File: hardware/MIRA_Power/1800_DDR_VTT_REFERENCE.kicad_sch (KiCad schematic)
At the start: 13 parts, among them Q1801 BSS138N, U1801 TPS51200DRCR

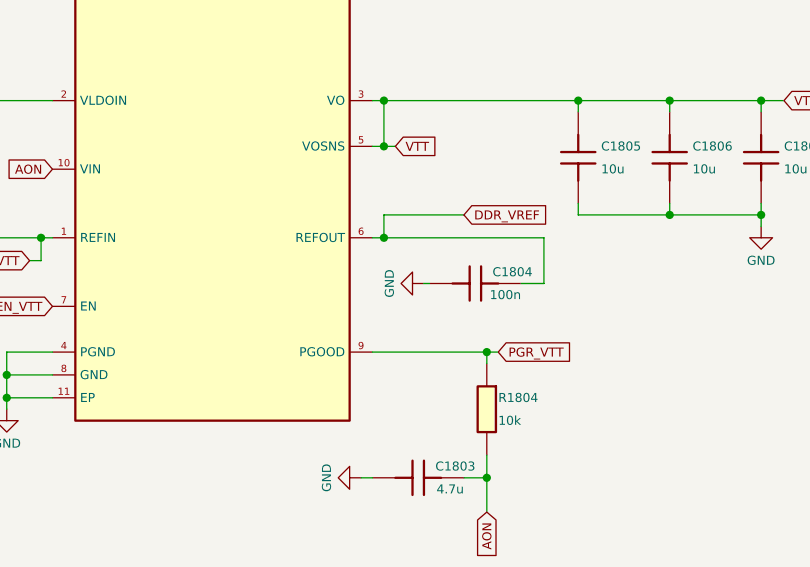
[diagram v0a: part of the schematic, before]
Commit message: Add high-load schematic candidate with CORE sense and revised N15 supply
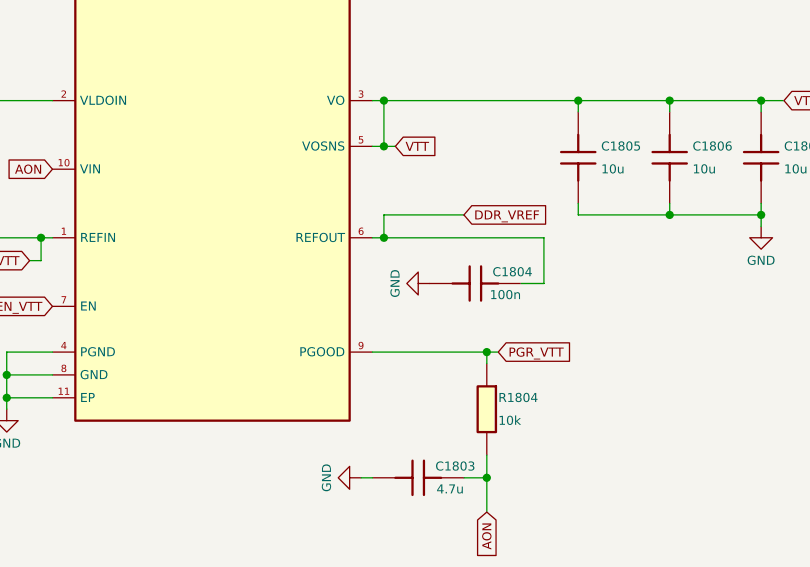
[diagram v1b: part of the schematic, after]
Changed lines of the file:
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@@
 	(wire
 		(pts
-			(xy 100.965 123.19) (xy 101.6 123.19)
+			(xy 101.6 123.19) (xy 101.6 123.19)
 		)
 		(stroke
@@
 	(symbol
 		(lib_id "power:GND")
-		(at 100.965 123.19 270)
+		(at 101.6 123.19 270)
 		(unit 1)
 		(body_style 1)
@@
 		(dnp no)
 		(property "Reference" "#PWR01805"
-			(at 100.965 123.19 0)
+			(at 101.6 123.19 0)
 			(hide yes)
 			(show_name no)
@@
 		)
 		(property "Value" "GND"
-			(at 97.155 123.19 0)
+			(at 97.79 123.19 0)
 			(show_name no)
 			(do_not_autoplace no)
@@
 		)
 		(property "Footprint" ""
-			(at 100.965 123.19 0)
+			(at 101.6 123.19 0)
 			(show_name no)
 			(do_not_autoplace no)
@@
 		)
 		(property "Datasheet" ""
-			(at 100.965 123.19 0)
+			(at 101.6 123.19 0)
 			(show_name no)
 			(do_not_autoplace no)
@@
 		)
 		(property "Description" ""
-			(at 100.965 123.19 0)
-			(show_name no)
-			(do_not_autoplace no)
+			(at 101.6 123.19 0)
+			(show_name no)
+			(do_not_autoplace no)

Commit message: Protect unpowered signal domains and qualify local supplies; retain startup and fault interlocks
MIRA-Startup-Patch: 7ffae17756ebcf923eff1212bb1aade8fbdfae03a9ca8ecebc69d3da3d3b4ba2
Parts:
- removed Q1801: BSS138N, MIRA_RevA:SOT-23, symbol MIRA_RevA:Q_BSS138NH6327XTSA2
- added R1805: 0R, MIRA_RevA:R_0201_Panasonic_ERJ1G_Gap0.30, symbol MIRA_RevA:R_ERJ1GN0R00C
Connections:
- net CMD_VTT: now also R1805.1
- net EN_VTT: now also R1805.2
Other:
- note added: "CMD_VTT is buffered on sheet 5300. R1805 links it directly to EN_VTT. DDR_VREF remains on with EN low."
- note added: "U1801 (TPS51200) uses AON for VIN and DDR1V35 for VLDOIN. The AUP buffer on sheet 5300 drives EN_VTT through R1805 without a VGS drop. R1801 and R5313 pull EN low when the buffer is disabled. Disabling EN discharges VTT; DDR_VREF remains active while its input supplies are valid."
- note removed: "CMD_VTT drives Q1801. R1801 pulls EN_VTT low. DDR_VREF remains on with EN low."
- note removed: "U1801 (TPS51200) uses AON for VIN and DDR1V35 for VLDOIN. Q1801 controls EN_VTT from CMD_VTT; R1801 (100 kOhm) pulls EN low when Q1801 is off. Disabling EN discharges VTT; DDR_VREF remains active while its input supplies are valid."
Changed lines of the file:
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@@
 		)
 	)
-	(text "CMD_VTT drives Q1801.\nR1801 pulls EN_VTT low.\nDDR_VREF remains on with EN low."
+	(text "CMD_VTT is buffered on sheet 5300.\nR1805 links it directly to EN_VTT.\nDDR_VREF remains on with EN low."
 		(exclude_from_sim no)
 		(at 73 40 0)
@@
 		)
 	)
-	(text "U1801 (TPS51200) uses AON for VIN and DDR1V35 for VLDOIN. Q1801 controls\nEN_VTT from CMD_VTT; R1801 (100 kOhm) pulls EN low when Q1801 is off.\nDisabling EN discharges VTT; DDR_VREF remains active while its input supplies\nare valid."
+	(text "U1801 (TPS51200) uses AON for VIN and DDR1V35 for VLDOIN. The AUP\nbuffer on sheet 5300 drives EN_VTT through R1805 without a VGS drop.\nR1801 and R5313 pull EN low when the buffer is disabled. Disabling EN\ndischarges VTT; DDR_VREF remains active while its input supplies are valid."
 		(exclude_from_sim no)
 		(at 156.21 65.3 0)
@@
 	(wire
 		(pts
-			(xy 35.56 48.26) (xy 36.83 48.26)
-		)
-		(stroke
-			(width 0)
-			(type default)
-		)
-	)
-	(wire
-		(pts
 			(xy 138.43 114.3) (xy 138.43 115.57)
 		)
@@
 	(wire
 		(pts
-			(xy 44.45 35.56) (xy 44.45 43.18)
-		)
-		(stroke
-			(width 0)
-			(type default)
-		)
-	)
-	(wire
-		(pts
 			(xy 58.42 120.65) (xy 58.42 118.11)
 		)
@@
 	(wire
 		(pts
-			(xy 40.64 35.56) (xy 44.45 35.56)
-		)
-		(stroke
-			(width 0)
-			(type default)
-		)
-	)
-	(wire
-		(pts
 			(xy 54.61 130.81) (xy 59.69 130.81)
 		)
@@
 	(wire
 		(pts
-			(xy 44.45 53.34) (xy 44.45 57.15)
-		)
-		(stroke
-			(width 0)
-			(type default)
-		)
-	)
-	(wire
-		(pts
 			(xy 93.98 144.78) (xy 95.25 144.78)
 		)
@@
 		)
 	)
-	(global_label "AON"
-		(shape input)
-		(at 40.64 35.56 180)
-		(effects
-			(font
-				(size 1 1)
-			)
-			(justify right)
-		)
-		(property "Intersheetrefs" "${INTERSHEET_REFS}"
-			(at 40.64 35.56 0)
-			(hide yes)
-			(show_name no)
-			(do_not_autoplace no)
-			(effects
-				(font
-					(size 1 1)
-				)
-			)
-		)
-	)
 	(global_label "DDR1V35"
 		(shape input)
@@
 		)
 	)
-	(global_label "CMD_VTT"
-		(shape input)
-		(at 35.56 48.26 180)
-		(effects
-			(font
-				(size 1 1)
-			)
-			(justify right)
-		)
-		(property "Intersheetrefs" "${INTERSHEET_REFS}"
-			(at 35.56 48.26 0)
-			(hide yes)
-			(show_name no)
-			(do_not_autoplace no)
-			(effects
-				(font
-					(size 1 1)
-				)
-			)
-		)
-	)
 	(global_label "EN_VTT"
 		(shape input)
@@
 	)
 	(symbol
-		(lib_id "MIRA_RevA:Q_BSS138NH6327XTSA2")
-		(at 41.91 48.26 0)
+		(lib_id "MIRA_RevA:R_ERJ1GN0R00C")
+		(at 39.37 48.26 0)
 		(unit 1)
-		(body_style 1)
 		(exclude_from_sim no)
 		(in_bom yes)
 		(on_board yes)
-		(in_pos_files yes)
 		(dnp no)
-		(property "Reference" "Q1801"
-			(at 50.8 46.99 0)
-			(show_name no)
-			(do_not_autoplace no)
+		(property "Reference" "R1805"
+			(at 39.37 44.26 0)
 			(effects
 				(font
-					(size 1 1)
+					(size 0.85 0.85)
 				)
 			)
 		)
-		(property "Value" "BSS138N"
-			(at 50.8 49.53 0)
-			(show_name no)
-			(do_not_autoplace no)
+		(property "Value" "0R"
+			(at 39.37 46.26 0)
 			(effects
 				(font
-					(size 1 1)
+					(size 0.85 0.85)
 				)
 			)
 		)
-		(property "Footprint" "MIRA_RevA:SOT-23"
-			(at 41.91 48.26 0)
+		(property "Footprint" "MIRA_RevA:R_0201_Panasonic_ERJ1G_Gap0.30"
+			(at 39.37 46.26 0)
 			(hide yes)
-			(show_name no)
-			(do_not_autoplace no)
 			(effects
 				(font
@@
 			)
 		)
-		(property "Datasheet" "https://www.infineon.com/part/BSS138N"
-			(at 41.91 48.26 0)
+		(property "Datasheet" ""
+			(at 39.37 46.26 0)
 			(hide yes)
-			(show_name no)
-			(do_not_autoplace no)
 			(effects
 				(font
@@
 			)
 		)
-		(property "Description" "N-channel MOSFET, 60V, SOT-23; supply-qualified enable source follower"
-			(at 41.91 48.26 0)
+		(property "MPN" "ERJ1GN0R00C"
+			(at 39.37 46.26 0)
 			(hide yes)
-			(show_name no)
-			(do_not_autoplace no)
 			(effects
 				(font
@@
 			)
 		)
-		(property "MPN" "BSS138NH6327XTSA2"
-			(at 41.91 48.26 0)
+		(property "Manufacturer" "Panasonic"
+			(at 39.37 46.26 0)
 			(hide yes)
-			(show_name no)
-			(do_not_autoplace no)
 			(effects
 				(font
@@
 			)
 		)
-		(property "Manufacturer" "Infineon"
-			(at 41.91 48.26 0)
+		(property "Description" "Zero-ohm jumper, 0201"
+			(at 39.37 46.26 0)
 			(hide yes)
-			(show_name no)
-			(do_not_autoplace no)
 			(effects
 				(font
@@
 		(pin "2"
 		)
-		(pin "3"
-		)
 		(instances
 			(project "MIRA_Power"
 				(path "/5c3dfbc0-84d7-4846-b0d0-d1c9bc7280bc/15ac01f5-4fbb-4009-99d1-55ed8240a53b/6cb14cfc-03f1-4f84-bc3d-825185ed9323/192298de-83f0-4b85-a128-d88097a24d4a"
-					(reference "Q1801")
+					(reference "R1805")
 					(unit 1)
 				)
@@
 		)
 	)
+	(wire
+		(pts
+			(xy 34.29 48.26)
+			(xy 31.75 48.26)
+		)
+		(stroke
+			(width 0)
+			(type default)
+		)
+	)
+	(global_label "CMD_VTT"
+		(shape bidirectional)
+		(at 31.75 48.26 180)
+		(effects
+			(font
+				(size 0.9 0.9)
+			)
+			(justify right)
+		)
+	)
+	(wire
+		(pts
+			(xy 44.45 48.26)
+			(xy 46.99 48.26)
+		)
+		(stroke
+			(width 0)
+			(type default)
+		)
+	)
+	(global_label "EN_VTT"
+		(shape bidirectional)
+		(at 46.99 48.26 0)
+		(effects
+			(font
+				(size 0.9 0.9)
+			)
+			(justify left)
+		)
+	)
